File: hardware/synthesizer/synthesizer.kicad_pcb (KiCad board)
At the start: 2 copper layers, 4 parts, among them J1 USB_C_Receptacle_PowerOnly_6P, J2 Conn_Coaxial, J3 Conn_Coaxial, U1 STM32H723VGTx

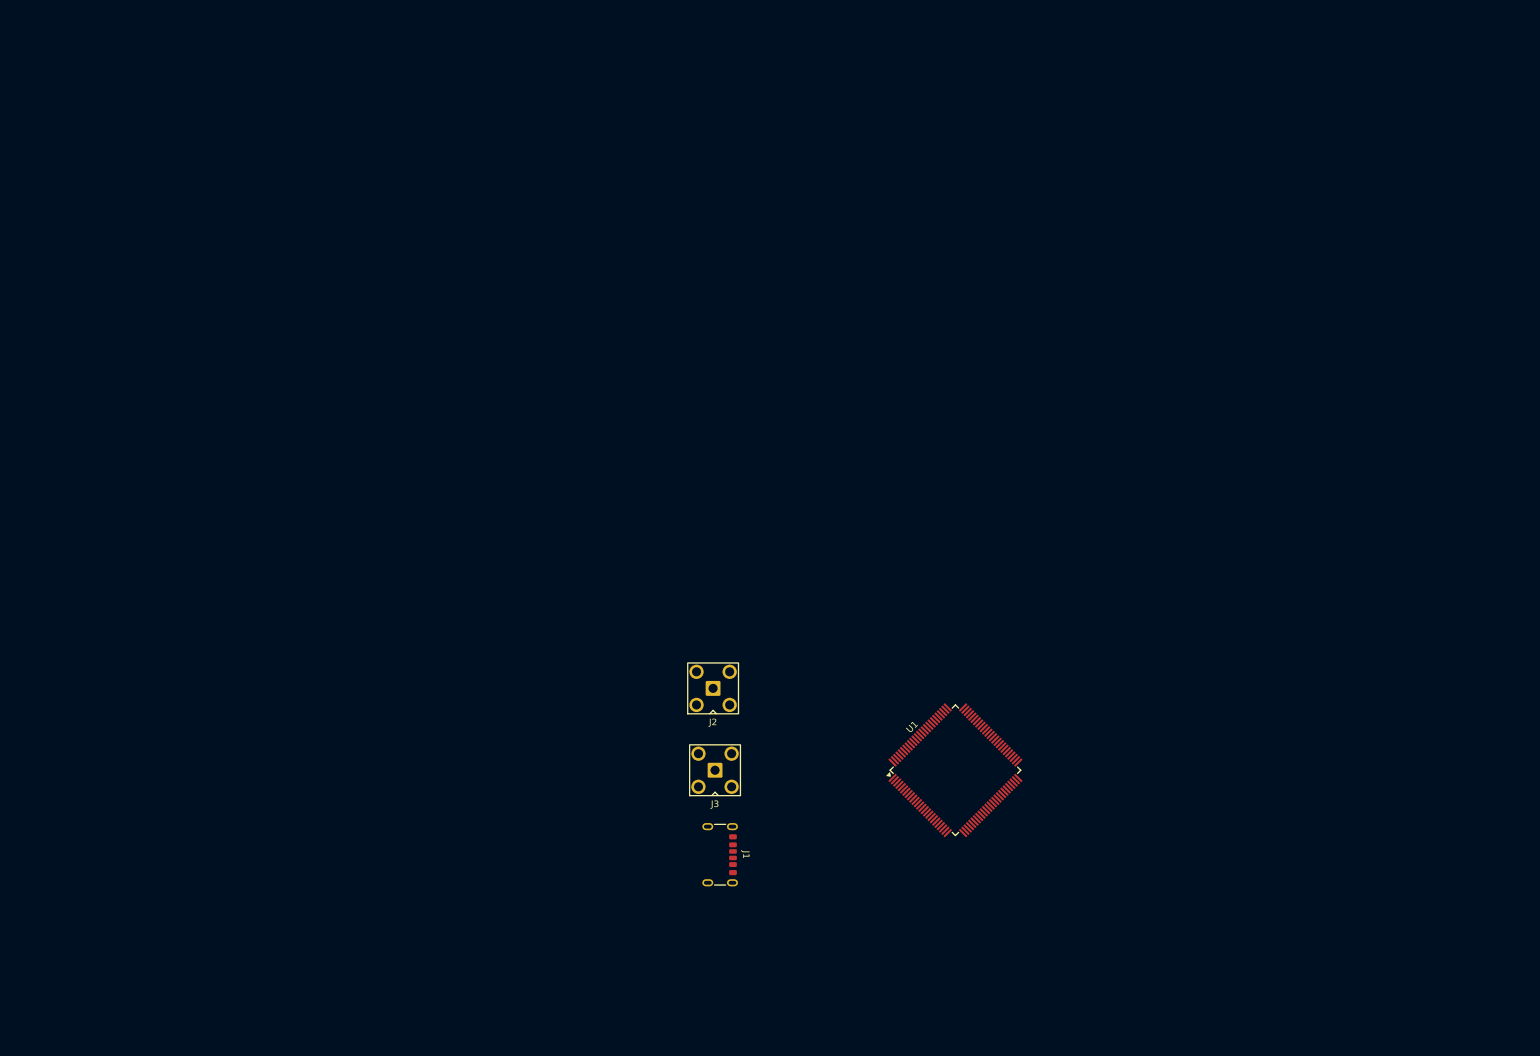
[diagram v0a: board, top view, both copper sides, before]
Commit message: add ethernet to synthesizer
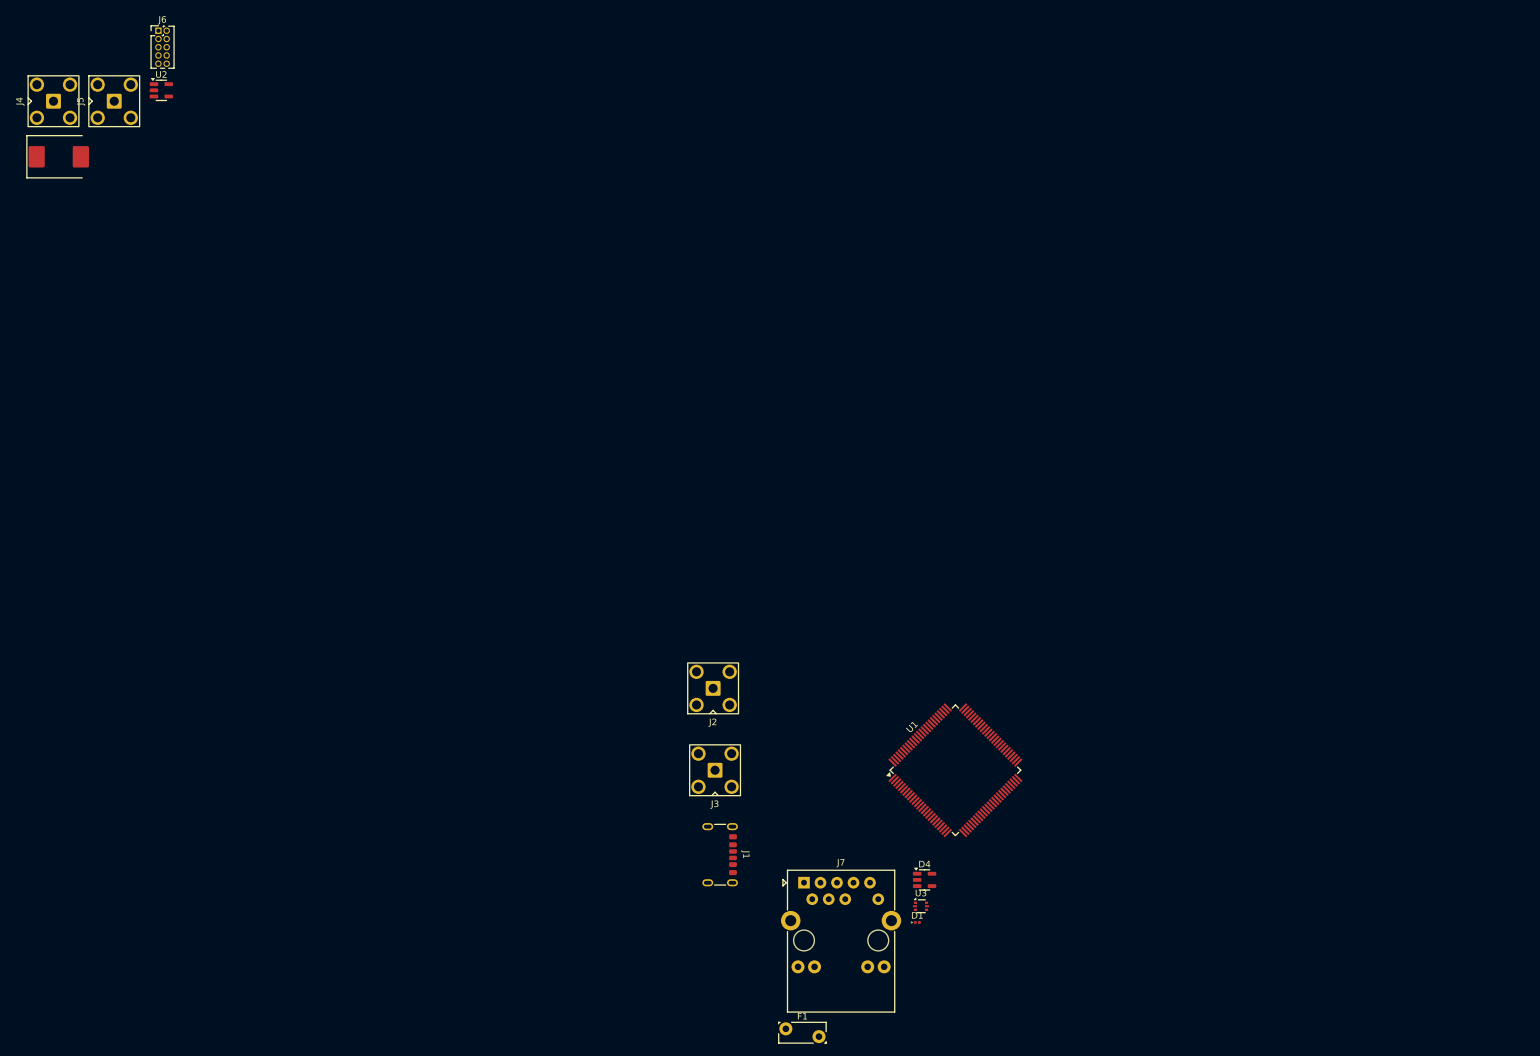
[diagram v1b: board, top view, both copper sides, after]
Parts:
- added D1: D, Diode_SMD:D_0201_0603Metric, F.Cu at (137.1, 138.4)
- added D4: ESDA6V1SC5, Package_TO_SOT_SMD:SOT-23-5, F.Cu at (138.2, 131.9)
- added D4: SMCJ6.5CA, PCM_JLCPCB:D_SMC, F.Cu at (4.99, 20.6)
- added F1: Polyfuse, Fuse:Fuse_Bourns_MF-RG300, F.Cu at (116.9, 154.8)
- added J4: Conn_Coaxial, Connector_Coaxial:SMA_BAT_Wireless_BWSMA-KWE-Z001, F.Cu at (4.17, 12.0)
- added J5: Conn_Coaxial, Connector_Coaxial:SMA_BAT_Wireless_BWSMA-KWE-Z001, F.Cu at (13.5, 12.0)
- added J6: Conn_ARM_JTAG_SWD_10, Connector_PinHeader_1.27mm:PinHeader_2x05_P1.27mm_Vertical, F.Cu at (20.3, 1.18)
- added J7: RJ45_Abracon_ARJP11A-MASA-B-A-EMU2, Connector_RJ:RJ45_Abracon_ARJP11A-MA_Horizontal, F.Cu at (119.7, 132.3)
- added U2: AP2112K-3.3, Package_TO_SOT_SMD:SOT-23-5, F.Cu at (20.8, 10.3)
- added U3: USBLC6-2P6, Package_TO_SOT_SMD:SOT-666, F.Cu at (137.7, 135.9)
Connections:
- net VBUS renamed Net-(F1-Pad1)
- U1 pad 10: Net-(U1-VSS-Pad10) -> GND
- U1 pad 19: unconnected-(U1-VSSA-Pad19) -> GND
- U1 pad 26: Net-(U1-VSS-Pad10) -> GND
- U1 pad 49: Net-(U1-VSS-Pad10) -> GND
- U1 pad 72: unconnected-(U1-PA13(JTMS-Pad72) -> /SWDIO
- U1 pad 74: Net-(U1-VSS-Pad10) -> GND
- U1 pad 76: unconnected-(U1-PA14(JTCK-Pad76) -> /SWCLK
- U1 pad 89: unconnected-(U1-PB3(JTDO-Pad89) -> /SWO
- U1 pad 99: Net-(U1-VSS-Pad10) -> GND

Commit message: created slides for cw8, split schematics
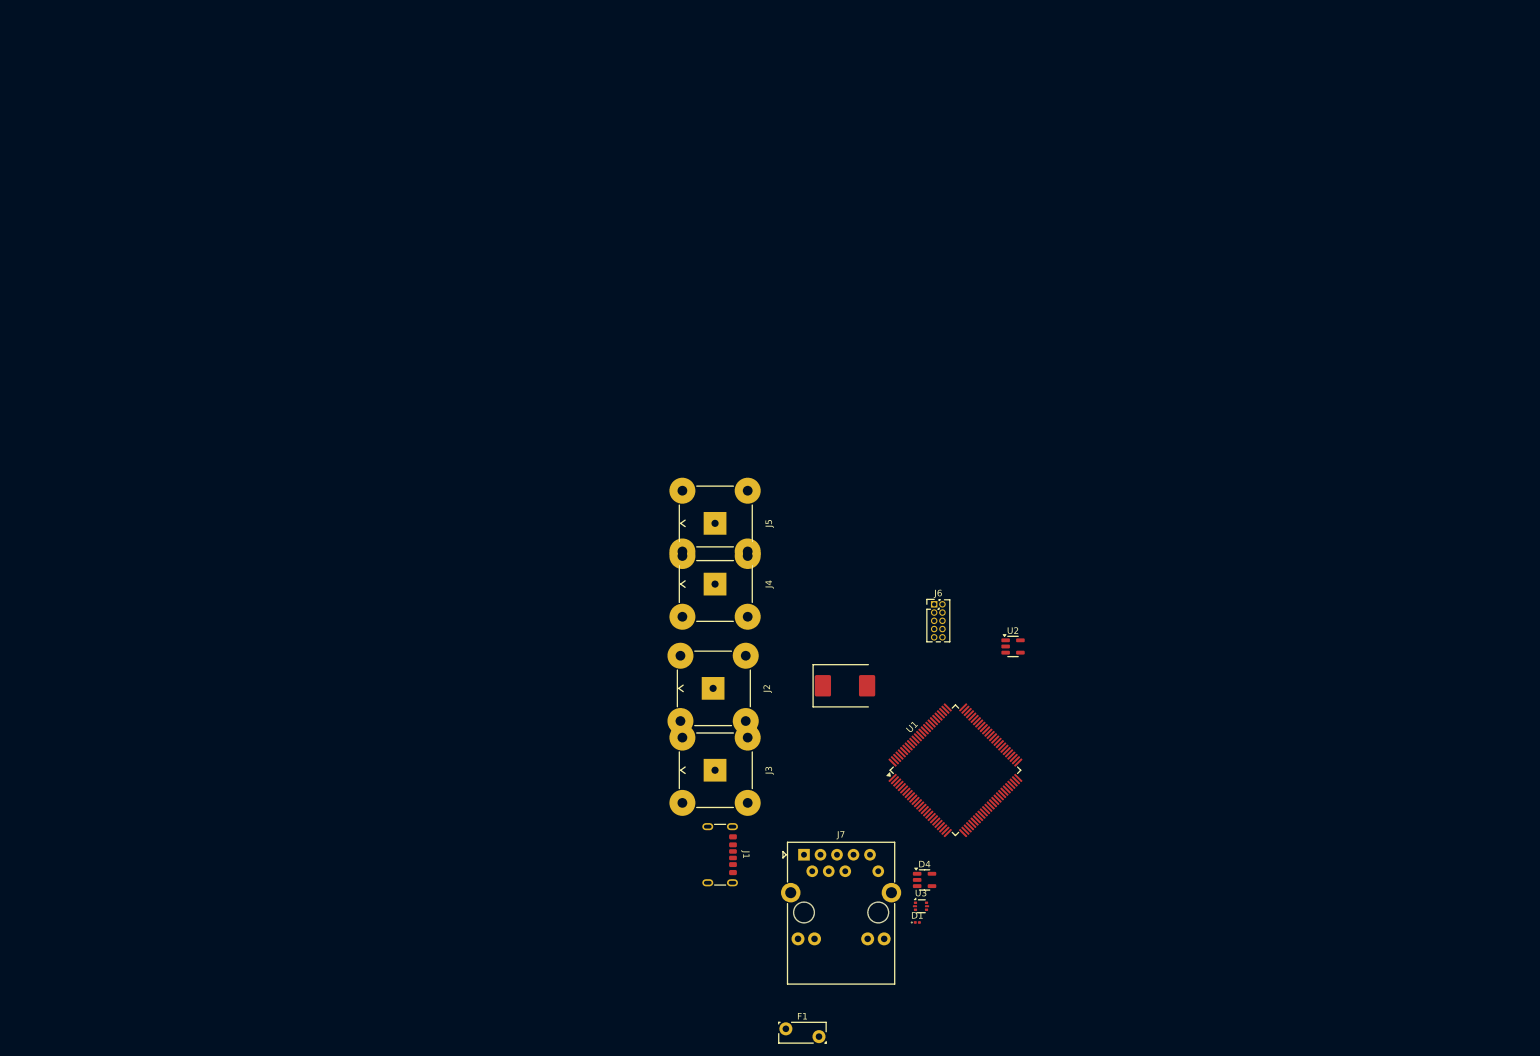
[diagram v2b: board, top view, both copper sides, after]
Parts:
- J2: value Conn_Coaxial -> Input 2; footprint Connector_Coaxial:SMA_BAT_Wireless_BWSMA-KWE-Z001 -> Connector_Coaxial:BNC_TEConnectivity_1478035_Horizontal
- J3: value Conn_Coaxial -> Input 1; footprint Connector_Coaxial:SMA_BAT_Wireless_BWSMA-KWE-Z001 -> Connector_Coaxial:BNC_TEConnectivity_1478035_Horizontal
- J4: value Conn_Coaxial -> Output 1; footprint Connector_Coaxial:SMA_BAT_Wireless_BWSMA-KWE-Z001 -> Connector_Coaxial:BNC_TEConnectivity_1478035_Horizontal
- J5: value Conn_Coaxial -> Output 2; footprint Connector_Coaxial:SMA_BAT_Wireless_BWSMA-KWE-Z001 -> Connector_Coaxial:BNC_TEConnectivity_1478035_Horizontal
- moved U2 156.6 mm to (151.9, 96.0)
- moved J6 148.5 mm to (139.7, 89.5)
- moved D4 145.9 mm to (126.0, 102.0)
- moved J4 126.1 mm to (106.0, 86.3), turned to 90 degrees
- moved J5 113.0 mm to (106.0, 77.0), turned to 90 degrees
- moved J7 4.31 mm to (119.7, 128.0)

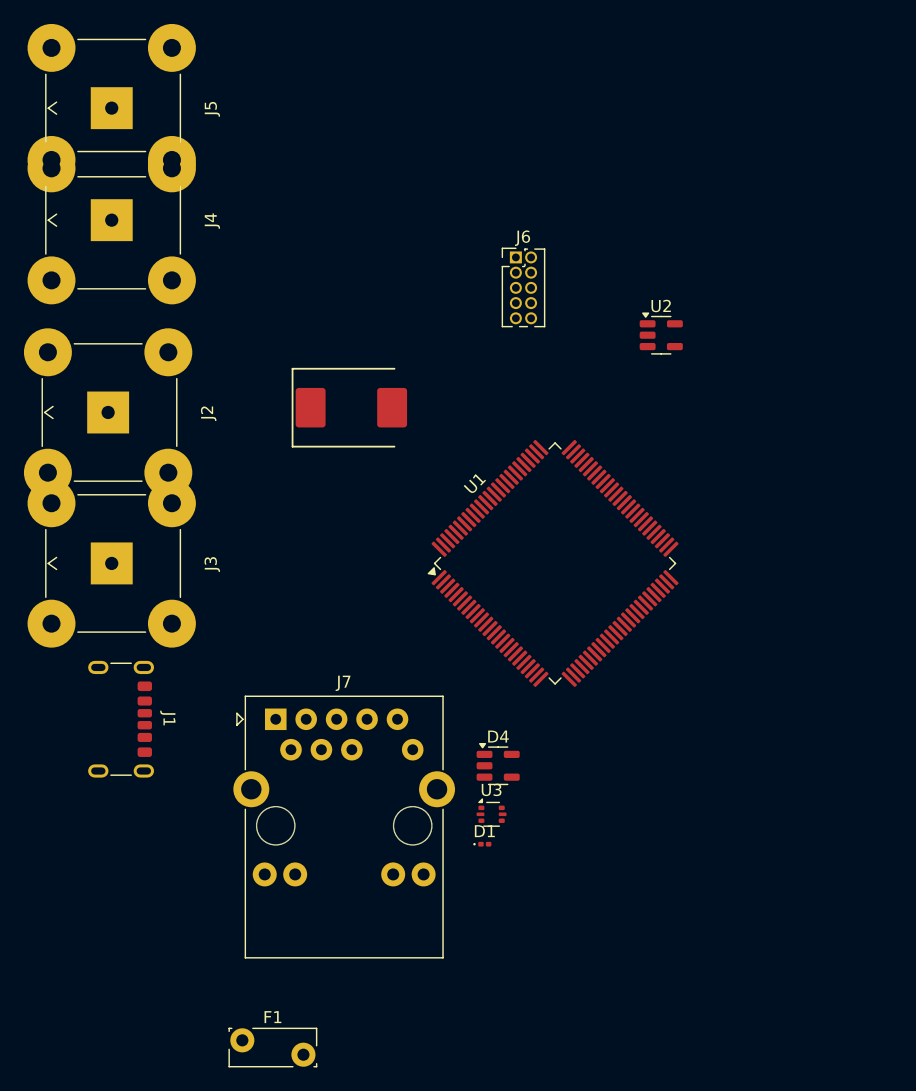
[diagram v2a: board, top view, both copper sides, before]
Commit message: finish ethernet jack
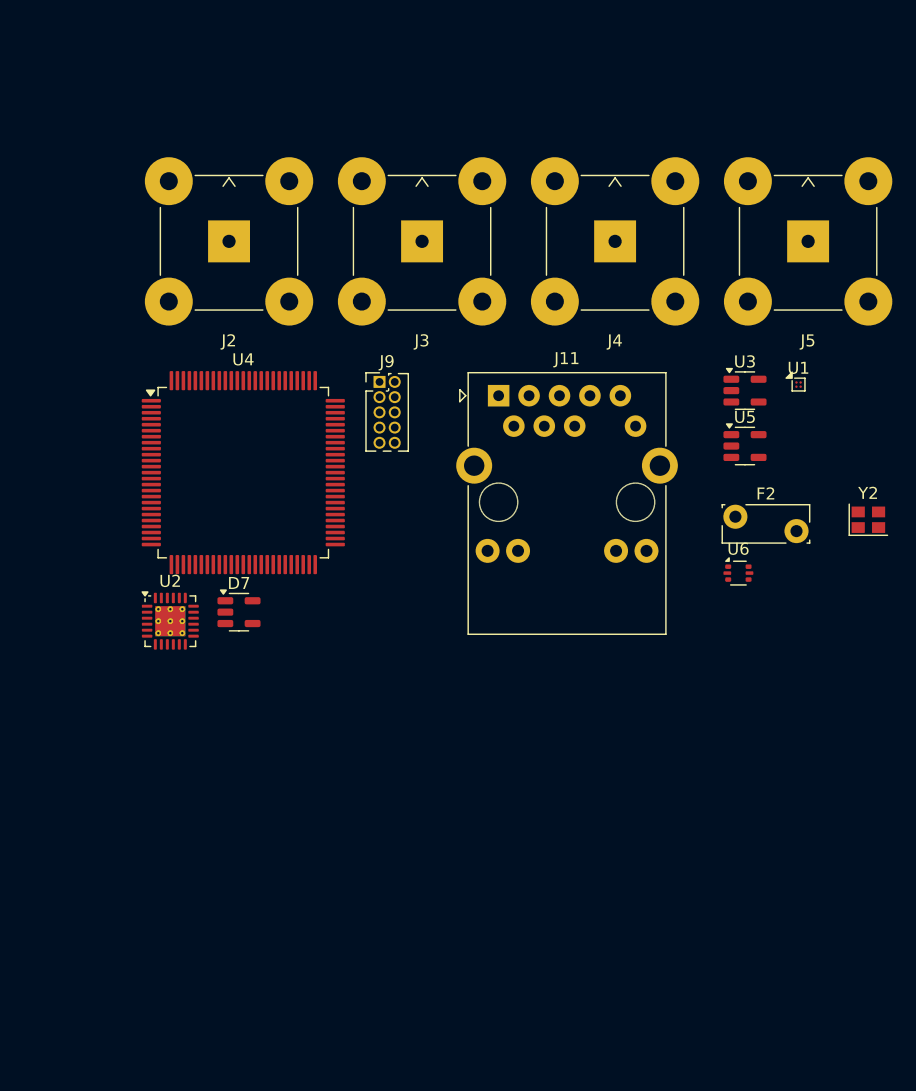
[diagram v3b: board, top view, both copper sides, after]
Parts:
- removed D1: D, Diode_SMD:D_0201_0603Metric
- removed D4: ESDA6V1SC5, Package_TO_SOT_SMD:SOT-23-5
- removed D4: SMCJ6.5CA, PCM_JLCPCB:D_SMC
- removed F1: Polyfuse, Fuse:Fuse_Bourns_MF-RG300
- removed J1: USB_C_Receptacle_PowerOnly_6P, Connector_USB:USB_C_Receptacle_GCT_USB4125-xx-x_6P_TopMnt_Horizontal
- removed J6: Conn_ARM_JTAG_SWD_10, Connector_PinHeader_1.27mm:PinHeader_2x05_P1.27mm_Vertical
- removed J7: RJ45_Abracon_ARJP11A-MASA-B-A-EMU2, Connector_RJ:RJ45_Abracon_ARJP11A-MA_Horizontal
- added D7: ESDA6V1SC5, Package_TO_SOT_SMD:SOT-23-5, F.Cu at (116.6, 119.1)
- added F2: Polyfuse, Fuse:Fuse_Bourns_MF-RG300, F.Cu at (158.1, 111.1)
- added J11: RJ45_Abracon_ARJP11A-MASA-B-A-EMU2, Connector_RJ:RJ45_Abracon_ARJP11A-MA_Horizontal, F.Cu at (138.3, 101.0)
- added J9: Conn_ARM_JTAG_SWD_10, Connector_PinHeader_1.27mm:PinHeader_2x05_P1.27mm_Vertical, F.Cu at (128.3, 99.8)
- added U4: STM32H723VGTx, Package_QFP:LQFP-100_14x14mm_P0.5mm, F.Cu at (117.0, 107.4)
- added U5: AP2112K-3.3, Package_TO_SOT_SMD:SOT-23-5, F.Cu at (158.8, 105.2)
- added U6: USBLC6-2P6, Package_TO_SOT_SMD:SOT-666, F.Cu at (158.3, 115.8)
- added Y2: SG-210STF, Oscillator:Oscillator_SMD_SeikoEpson_SG210-4Pin_2.5x2.0mm, F.Cu at (169.2, 111.3)
- U1: value STM32H723VGTx -> MAX40200ANS; footprint Package_QFP:LQFP-100_14x14mm_P0.5mm -> Package_BGA:WLP-4_0.728x0.728mm_Layout2x2_P0.35mm
- U2: value AP2112K-3.3 -> LAN8742A; footprint Package_TO_SOT_SMD:SOT-23-5 -> Package_DFN_QFN:VQFN-24-1EP_4x4mm_P0.5mm_EP2.5x2.5mm_ThermalVias
- U3: value USBLC6-2P6 -> AP2112K-1.2; footprint Package_TO_SOT_SMD:SOT-666 -> Package_TO_SOT_SMD:SOT-23-5
- moved J5 59.2 mm to (164.1, 88.1), turned to 0 degrees
- moved U2 47.4 mm to (110.9, 119.8)
- moved J4 42.0 mm to (148.0, 88.1), turned to 0 degrees
- moved U3 41.2 mm to (158.8, 100.6)
- moved J3 37.3 mm to (131.9, 88.1), turned to 0 degrees
- moved U1 25.2 mm to (163.3, 100.1), turned to 0 degrees
- moved J2 17.5 mm to (115.8, 88.1), turned to 0 degrees
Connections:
- U2 pad 1: +5V -> +3.3V
- U2 pad 2: GND -> Net-(U2-LED2/~{INTSEL})
- U2 pad 3: +5V -> Net-(U2-LED1/REGOFF)
- U2 pad 5: +3.3V -> /Clocks/25MHz
- U3 pad 1: USB+ -> +5V
- U3 pad 3: USB- -> +5V
- U3 pad 5: VBUS -> +1.2V

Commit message: further improvements
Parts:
- removed J2: Input 2, Connector_Coaxial:BNC_TEConnectivity_1478035_Horizontal
- removed J3: Input 1, Connector_Coaxial:BNC_TEConnectivity_1478035_Horizontal
- removed J4: Output 1, Connector_Coaxial:BNC_TEConnectivity_1478035_Horizontal
- removed J5: Output 2, Connector_Coaxial:BNC_TEConnectivity_1478035_Horizontal
- added J1: Conn_ARM_SWD_TagConnect_TC2030, Connector:Tag-Connect_TC2030-IDC-FP_2x03_P1.27mm_Vertical, F.Cu at (141.1, 98.0)
- added J10: Output 2, Connector_Coaxial:BNC_TEConnectivity_1478035_Horizontal, F.Cu at (174.2, 83.1)
- added J6: Input 1, Connector_Coaxial:BNC_TEConnectivity_1478035_Horizontal, F.Cu at (125.9, 83.1)
- added J7: Input 2, Connector_Coaxial:BNC_TEConnectivity_1478035_Horizontal, F.Cu at (142.0, 83.1)
- J9: value Conn_ARM_JTAG_SWD_10 -> Output 1; footprint Connector_PinHeader_1.27mm:PinHeader_2x05_P1.27mm_Vertical -> Connector_Coaxial:BNC_TEConnectivity_1478035_Horizontal
- U4: value STM32H723VGTx -> STM32H723VGT6
- moved J9 34.1 mm to (158.1, 83.1)
- moved U2 31.8 mm to (139.5, 105.9)
- moved D7 23.6 mm to (138.9, 111.4)
- moved J11 14.5 mm to (151.9, 96.0)
- moved U1 14.5 mm to (177.0, 95.1)
- moved U3 14.5 mm to (172.5, 95.6)
- moved U5 14.5 mm to (172.5, 100.2)
- moved F2 14.5 mm to (171.7, 106.1)
- moved U6 14.5 mm to (171.9, 110.8)
- moved U4 11.3 mm to (127.1, 102.4)
- moved Y2 5.83 mm to (172.2, 116.3)
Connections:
- D7 pad 5: Net-(J9-~{RESET}) -> /Microcontroller/SWD_NRST
- J9 pad 1: +3.3V -> unconnected-(J9-In-Pad1)
- J9 pad 2: /Microcontroller/SWDIO -> GND
- U4 pad 14: Net-(U4-NRST) -> /Microcontroller/SWD_NRST
- U4 pad 48: unconnected-(U4-VCAP-Pad48) -> Net-(C22-Pad1)
- U4 pad 73: unconnected-(U4-VCAP-Pad73) -> Net-(C30-Pad1)
- U4 pad 8: unconnected-(U4-PC14-Pad8) -> Net-(U4-PC14)
- U4 pad 9: unconnected-(U4-PC15-Pad9) -> Net-(U4-PC15)
- U4 pad 94: GND -> Net-(U4-BOOT0)
